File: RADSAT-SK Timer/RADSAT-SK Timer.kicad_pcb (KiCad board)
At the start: 2 copper layers, 90.2 x 95.9 mm, 97 parts, among them J101 Conn_02x26_Odd_Even, J103 Conn_02x26_Odd_Even, J201 Conn_01x04, J203 Conn_01x02, J204 USB_B_Micro, Q101 IRLML2060, Q102 IRLML2060, Q103 IRLML2060, Q104 IRLML2060, Q105 IRLML2060, Q106 IRLML2060, Q107 IRLML2060, Q108 IRLML2060, Q109 IRLML2060, Q201 IRLML2060, SW201 SW_Push, SW202 SW_Push, SW203 SW_Push, SW204 SW_Push, SW205 SW_Push, SW206 SW_Push, U101 LM397MF, U102 LM397MF, U103 LM397MF, U104 CD4052B, U202 LTC3440EMSPBF

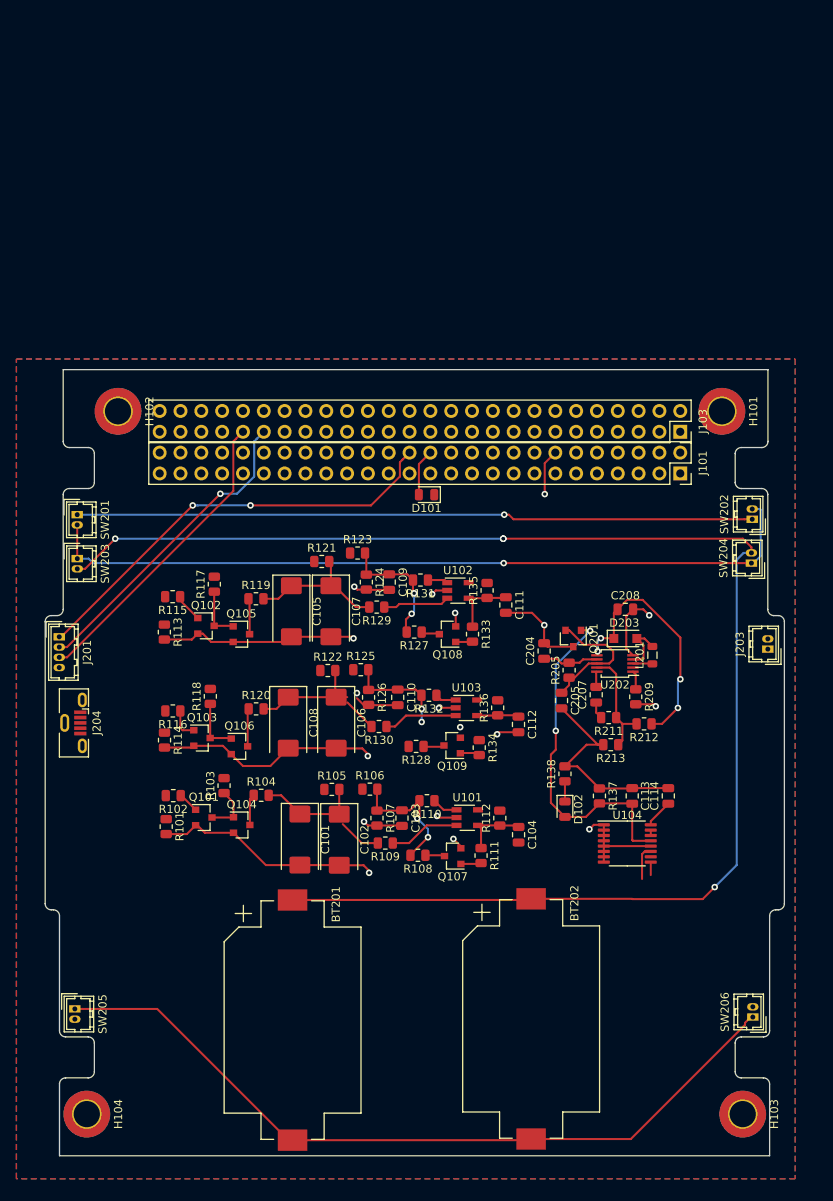
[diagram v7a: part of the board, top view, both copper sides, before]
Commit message: Retrace (#10)
* Schematic: Added- 2 more inhibit ports Added- RBF Ports In and Out Connected USb Charger to connector H1-32. Layout: Port positioning and adjustments to some existing circuitry for better tracing.

* schematic saved with above changes

* Retraced the board

* added starting place for RBF timer

* Mason has updated some footprints

* Change to the 7 pin Antenna on the PCB

* added RBF stuff to PCB

* moved some traces

Co-authored-by: Arthur Nemetz <arn725@usask.ca>
Co-authored-by: Addi Amaya <caa746@usask.ca>
Co-authored-by: Mason <mdl446@mail.usask.ca>
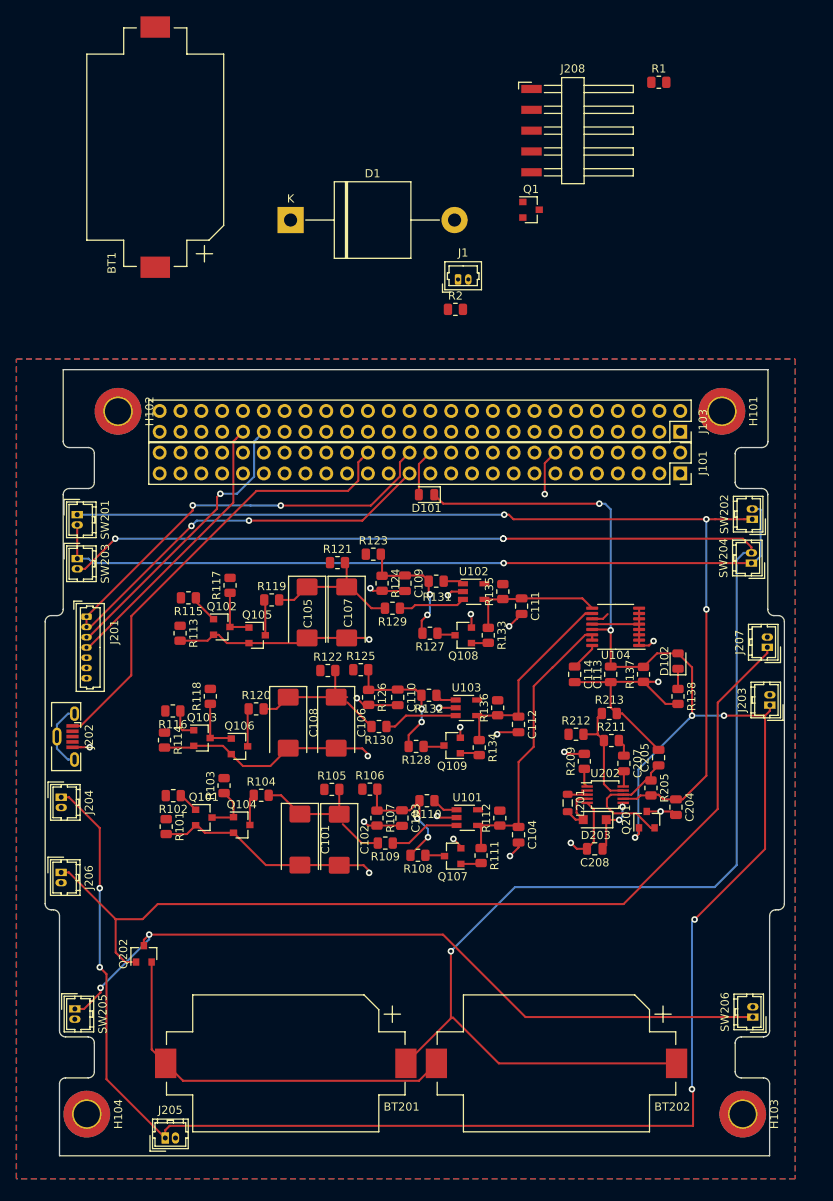
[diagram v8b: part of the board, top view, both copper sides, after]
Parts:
- added BT1: Battery_Cell, Battery:BatteryHolder_Keystone_1060_1x2032, F.Cu at (48.3, 22.9)
- added D1: 5KPxxA, Diode_THT:D_P600_R-6_P20.00mm_Horizontal, F.Cu at (64.8, 31.8)
- added J1: Conn_01x02_Male, Connector_Molex:Molex_PicoBlade_53047-0210_1x02_P1.25mm_Vertical, F.Cu at (85.2, 39.0)
- added J202: USB_B_Micro, Connector_USB:USB_Micro-B_Molex-105133-0001, F.Cu at (37.3, 94.8)
- added J205: Conn_01x02, Connector_Hirose:Hirose_DF13-02P-1.25DSA_1x02_P1.25mm_Vertical, F.Cu at (49.5, 143.7)
- added J206: Conn_01x02, Connector_Hirose:Hirose_DF13-02P-1.25DSA_1x02_P1.25mm_Vertical, F.Cu at (36.8, 111.3)
- added J207: Conn_01x02, Connector_Hirose:Hirose_DF13-02P-1.25DSA_1x02_P1.25mm_Vertical, F.Cu at (122.9, 83.9)
- added J208: Conn_01x05_Male, Connector_Harwin:Harwin_M20-89005xx_1x05_P2.54mm_Horizontal, F.Cu at (99.7, 20.8)
- added Q1: Q_NMOS_DGS, Package_TO_SOT_SMD:SOT-23, F.Cu at (94.1, 30.5)
- added Q202: IRLML2060, Package_TO_SOT_SMD:SOT-23, F.Cu at (46.9, 121.3)
- added R1: R, Resistor_SMD:R_0805_2012Metric, F.Cu at (109.7, 14.9)
- added R2: R, Resistor_SMD:R_0805_2012Metric, F.Cu at (84.9, 42.6)
- J201: value Conn_01x04 -> Conn_01x07; footprint Connector_Hirose:Hirose_DF13-04P-1.25DSA_1x04_P1.25mm_Vertical -> Connector_Molex:Molex_PicoBlade_53047-0710_1x07_P1.25mm_Vertical
- J204: value USB_B_Micro -> Conn_01x02; footprint Connector_USB:USB_Micro-B_Molex-105133-0001 -> Connector_Hirose:Hirose_DF13-02P-1.25DSA_1x02_P1.25mm_Vertical
- moved C208 29.4 mm to (101.9, 108.4), turned to 180 degrees
- moved U104 26.5 mm to (104.4, 81.4), turned to 180 degrees
- moved C204 24.9 mm to (111.8, 103.4), turned to 270 degrees
- moved Q201 23.8 mm to (108.2, 104.9), turned to 90 degrees
- moved D102 22.7 mm to (112.0, 85.5), turned to 90 degrees
- moved D203 22.4 mm to (101.9, 104.9), turned to 180 degrees
- moved L201 20.8 mm to (98.6, 102.9), turned to 270 degrees
- moved C114 18.7 mm to (99.4, 87.2), turned to 270 degrees
- moved R205 17.5 mm to (108.7, 101.0), turned to 270 degrees
- moved R138 16.7 mm to (112.0, 89.9), turned to 270 degrees
- moved U202 16.0 mm to (103.1, 101.8), turned to 0 degrees
- moved R137 15.8 mm to (107.8, 87.2), turned to 90 degrees
- moved C113 15.1 mm to (103.8, 87.2), turned to 270 degrees
- moved C205 13.7 mm to (109.7, 97.3), turned to 90 degrees
- moved R209 10.1 mm to (100.6, 97.8), turned to 90 degrees
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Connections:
- J101 pad 1: (no net) -> Net-(J101-Pad1)
- J101 pad 10: (no net) -> Net-(J101-Pad10)
- J101 pad 11: (no net) -> Net-(J101-Pad11)
- J101 pad 12: (no net) -> Net-(J101-Pad12)
- J101 pad 13: (no net) -> Net-(J101-Pad13)
- J101 pad 15: (no net) -> Net-(J101-Pad15)
- J101 pad 16: (no net) -> Net-(J101-Pad16)
- J101 pad 17: (no net) -> Net-(J101-Pad17)
- J101 pad 18: (no net) -> Net-(J101-Pad18)
- J101 pad 19: (no net) -> Net-(J101-Pad19)
- J101 pad 2: (no net) -> Net-(J101-Pad2)
- J101 pad 20: (no net) -> Net-(J101-Pad20)
- J101 pad 21: (no net) -> Net-(J101-Pad21)
- J101 pad 22: (no net) -> Net-(J101-Pad22)
- J101 pad 23: (no net) -> Net-(J101-Pad23)
- J101 pad 24: (no net) -> Net-(J101-Pad24)
- J101 pad 25: (no net) -> Net-(J101-Pad25)
- J101 pad 27: (no net) -> Net-(J101-Pad27)
- J101 pad 29: (no net) -> Net-(J101-Pad29)
- J101 pad 3: (no net) -> Net-(J101-Pad3)
- J101 pad 30: (no net) -> Net-(J101-Pad30)
- J101 pad 31: (no net) -> Net-(J101-Pad31)
- J101 pad 32: (no net) -> Net-(J101-Pad32)
- J101 pad 33: (no net) -> Net-(J101-Pad33)
- J101 pad 34: (no net) -> Net-(J101-Pad34)
- J101 pad 35: (no net) -> Net-(J101-Pad35)
- J101 pad 36: (no net) -> Net-(J101-Pad36)
- J101 pad 37: (no net) -> Net-(J101-Pad37)
- J101 pad 38: (no net) -> Net-(J101-Pad38)
- J101 pad 39: (no net) -> Net-(J101-Pad39)
- J101 pad 4: (no net) -> Net-(J101-Pad4)
- J101 pad 40: (no net) -> Net-(J101-Pad40)
- J101 pad 41: (no net) -> Net-(J101-Pad41)
- J101 pad 42: (no net) -> Net-(J101-Pad42)
- J101 pad 43: (no net) -> Net-(J101-Pad43)
- J101 pad 44: (no net) -> Net-(J101-Pad44)
- J101 pad 45: (no net) -> Net-(J101-Pad45)
- J101 pad 46: (no net) -> Net-(J101-Pad46)
- J101 pad 47: (no net) -> Net-(J101-Pad47)
- J101 pad 48: (no net) -> Net-(J101-Pad48)
- J101 pad 49: (no net) -> Net-(J101-Pad49)
- J101 pad 5: (no net) -> Net-(J101-Pad5)
- J101 pad 50: (no net) -> Net-(J101-Pad50)
- J101 pad 51: (no net) -> Net-(J101-Pad51)
- J101 pad 52: (no net) -> Net-(J101-Pad52)
- J101 pad 6: (no net) -> Net-(J101-Pad6)
- J101 pad 7: (no net) -> Net-(J101-Pad7)
- J101 pad 8: (no net) -> Net-(J101-Pad8)
- J101 pad 9: (no net) -> Net-(J101-Pad9)
- J103 pad 1: (no net) -> Net-(J103-Pad1)
- J103 pad 10: (no net) -> Net-(J103-Pad10)
- J103 pad 11: (no net) -> Net-(J103-Pad11)
- J103 pad 12: (no net) -> Net-(J103-Pad12)
- J103 pad 13: (no net) -> Net-(J103-Pad13)
- J103 pad 14: (no net) -> Net-(J103-Pad14)
- J103 pad 15: (no net) -> Net-(J103-Pad15)
- J103 pad 16: (no net) -> Net-(J103-Pad16)
- J103 pad 17: (no net) -> Net-(J103-Pad17)
- J103 pad 18: (no net) -> Net-(J103-Pad18)
- J103 pad 19: (no net) -> Net-(J103-Pad19)
- J103 pad 2: (no net) -> Net-(J103-Pad2)
- J103 pad 20: (no net) -> Net-(J103-Pad20)
- J103 pad 21: (no net) -> Net-(J103-Pad21)
- J103 pad 22: (no net) -> Net-(J103-Pad22)
- J103 pad 23: (no net) -> Net-(J103-Pad23)
- J103 pad 24: (no net) -> Net-(J103-Pad24)
- J103 pad 25: (no net) -> Net-(J103-Pad25)
- J103 pad 26: (no net) -> Net-(J103-Pad26)
- J103 pad 27: (no net) -> Net-(J103-Pad27)
- J103 pad 28: (no net) -> Net-(J103-Pad28)
- J103 pad 29: (no net) -> Net-(J103-Pad29)
- J103 pad 3: (no net) -> Net-(J103-Pad3)
- J103 pad 30: (no net) -> Net-(J103-Pad30)
- J103 pad 31: (no net) -> Net-(J103-Pad31)
- J103 pad 32: (no net) -> Net-(J103-Pad32)
- J103 pad 33: (no net) -> Net-(J103-Pad33)
- J103 pad 34: (no net) -> Net-(J103-Pad34)
- J103 pad 35: (no net) -> Net-(J103-Pad35)
- J103 pad 36: (no net) -> Net-(J103-Pad36)
- J103 pad 37: (no net) -> Net-(J103-Pad37)
- J103 pad 38: (no net) -> Net-(J103-Pad38)
- J103 pad 39: (no net) -> Net-(J103-Pad39)
- J103 pad 4: (no net) -> Net-(J103-Pad4)
- J103 pad 40: (no net) -> Net-(J103-Pad40)
- J103 pad 42: (no net) -> Net-(J103-Pad42)
- J103 pad 44: (no net) -> Net-(J103-Pad44)
- J103 pad 45: (no net) -> Net-(J103-Pad45)
- J103 pad 46: (no net) -> Net-(J103-Pad46)
- J103 pad 47: (no net) -> Net-(J103-Pad47)
- J103 pad 48: (no net) -> Net-(J103-Pad48)
- J103 pad 49: (no net) -> Net-(J103-Pad49)
- J103 pad 5: (no net) -> Net-(J103-Pad5)
- J103 pad 50: (no net) -> Net-(J103-Pad50)
- J103 pad 51: (no net) -> Net-(J103-Pad51)
- J103 pad 52: (no net) -> Net-(J103-Pad52)
- J103 pad 6: (no net) -> Net-(J103-Pad6)
- J103 pad 7: (no net) -> Net-(J103-Pad7)
- J103 pad 8: (no net) -> Net-(J103-Pad8)
- J103 pad 9: (no net) -> Net-(J103-Pad9)
- J201 pad 2: I2C_DATA -> +3V3
- J201 pad 3: I2C_CLK -> I2C_DATA
- J201 pad 4: GND -> I2C_CLK
- J204 pad 1: (no net) -> BUS_EN
- J204 pad 2: (no net) -> GND
- SW205 pad 1: Net-(BT201-Pad2) -> Net-(Q202-Pad3)
- SW206 pad 1: Net-(BT201-Pad2) -> Net-(Q202-Pad3)
- U202 pad 2: (no net) -> Net-(U202-Pad2)
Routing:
- net BUS_EN: track 42.2 -> 257.3 mm, vias 2 -> 9
- net /RADSAT-SK Timer 2/RBF: track 0.00 -> 117.3 mm
- net Net-(Q202-Pad3): track 0.00 -> 94.2 mm, vias 0 -> 2
- net USB_Charge: track 0.00 -> 55.4 mm
- net Net-(BT201-Pad2): track 95.7 -> 47.8 mm
- net +3V3: track 53.1 -> 97.5 mm, vias 2 -> 4
- net Net-(C204-Pad1): track 89.5 -> 125.6 mm, vias 1 -> 3
- net Net-(BT201-Pad1): track 180.3 -> 209.3 mm
- net Timer_A_out: track 8.59 -> 36.6 mm
- net +BATT: track 38.2 -> 14.0 mm, vias 4 -> 2
- net Timer_C_out: track 5.18 -> 25.1 mm
- net Net-(J202-Pad6): track 0.00 -> 8.32 mm
- net Timer_B_out: track 9.83 -> 17.4 mm
- net Net-(C110-Pad1): track 12.3 -> 15.9 mm
- net I2C_CLK: track 37.3 -> 34.4 mm
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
